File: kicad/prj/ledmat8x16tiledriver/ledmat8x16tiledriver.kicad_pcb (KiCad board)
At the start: 4 copper layers, 31.9 x 31.9 mm, 15 parts, among them J3 Conn_02x08_Odd_Even, J4 Conn_02x08_Odd_Even, U2 DMP31D7LDW, U3 DMP31D7LDW, U4 DMP31D7LDW, U5 DMP31D7LDW

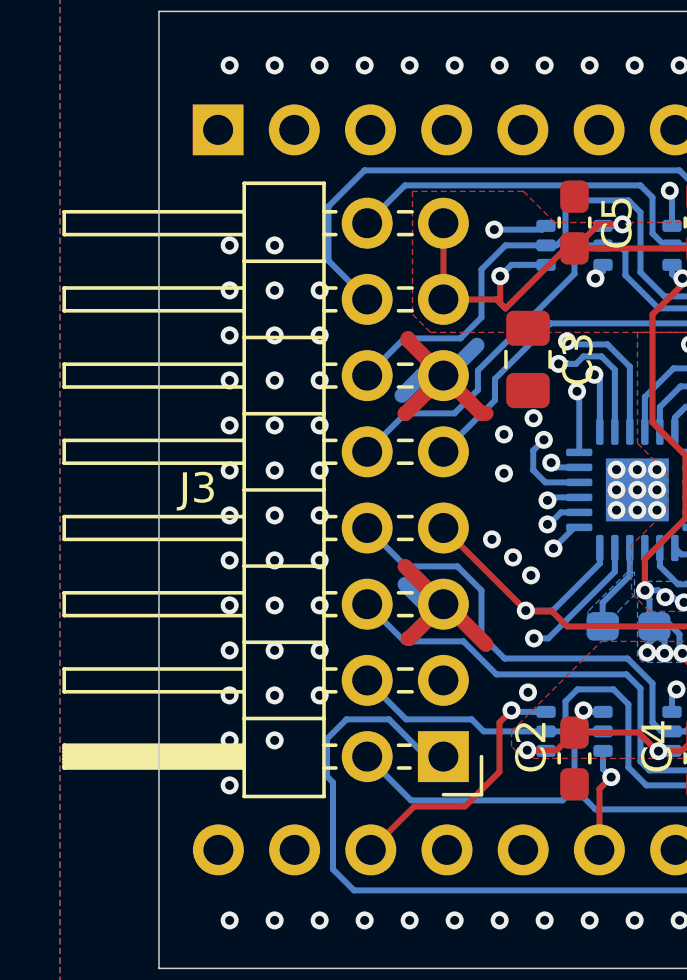
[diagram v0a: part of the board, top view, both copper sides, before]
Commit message: Update footprints in layout (including the led matrix module one)
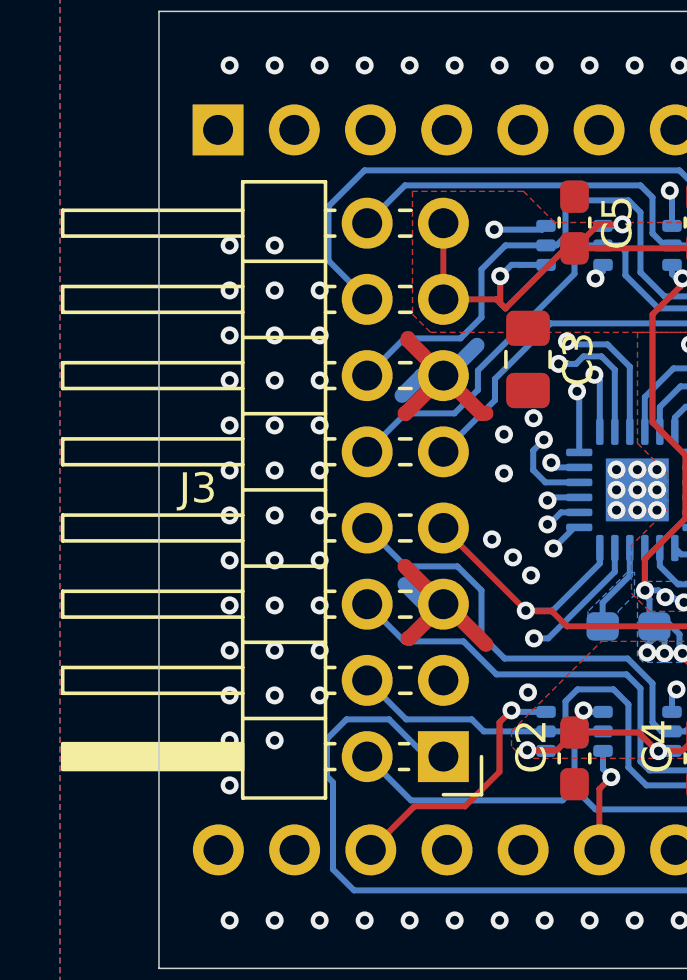
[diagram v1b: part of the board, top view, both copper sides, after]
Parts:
- U1: value ~ -> TLC59283

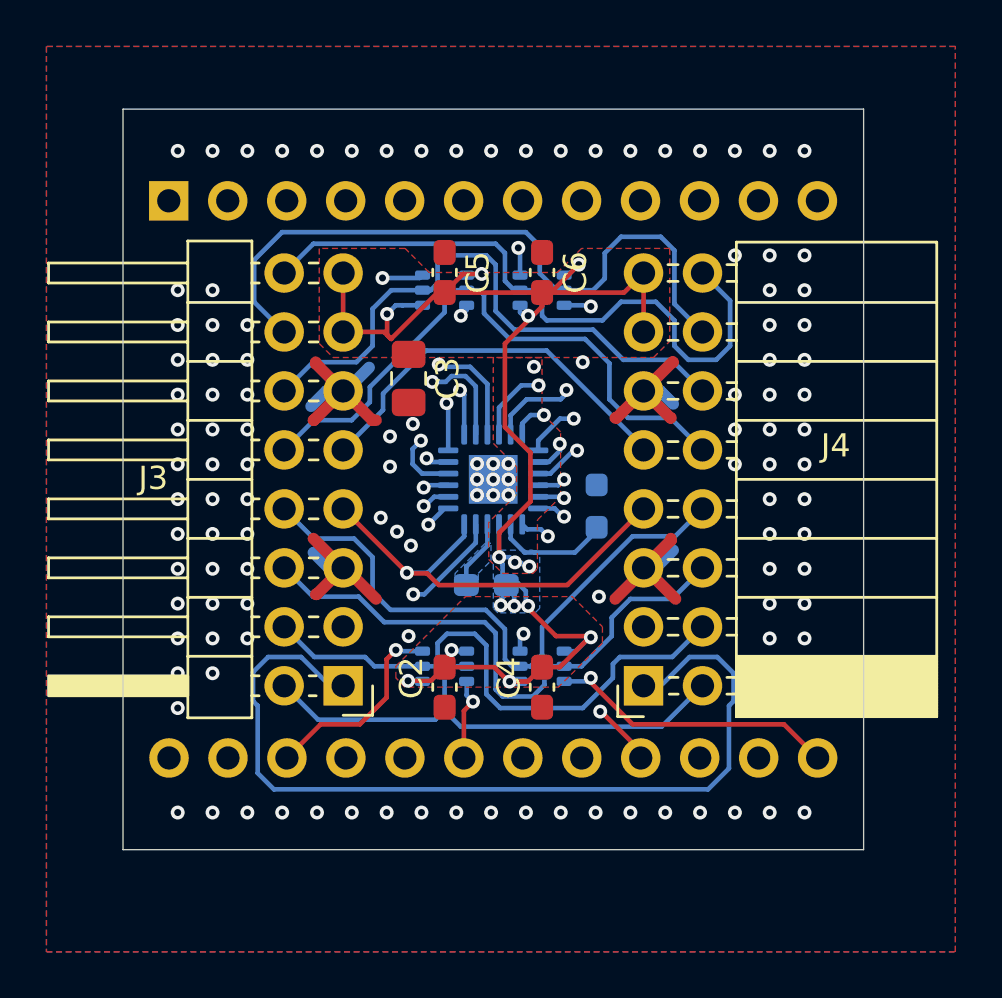
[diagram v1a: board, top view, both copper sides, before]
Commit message: Cut little arcs into the corners for mounting modules with maybe M3 screws
Or perhaps standoffs?
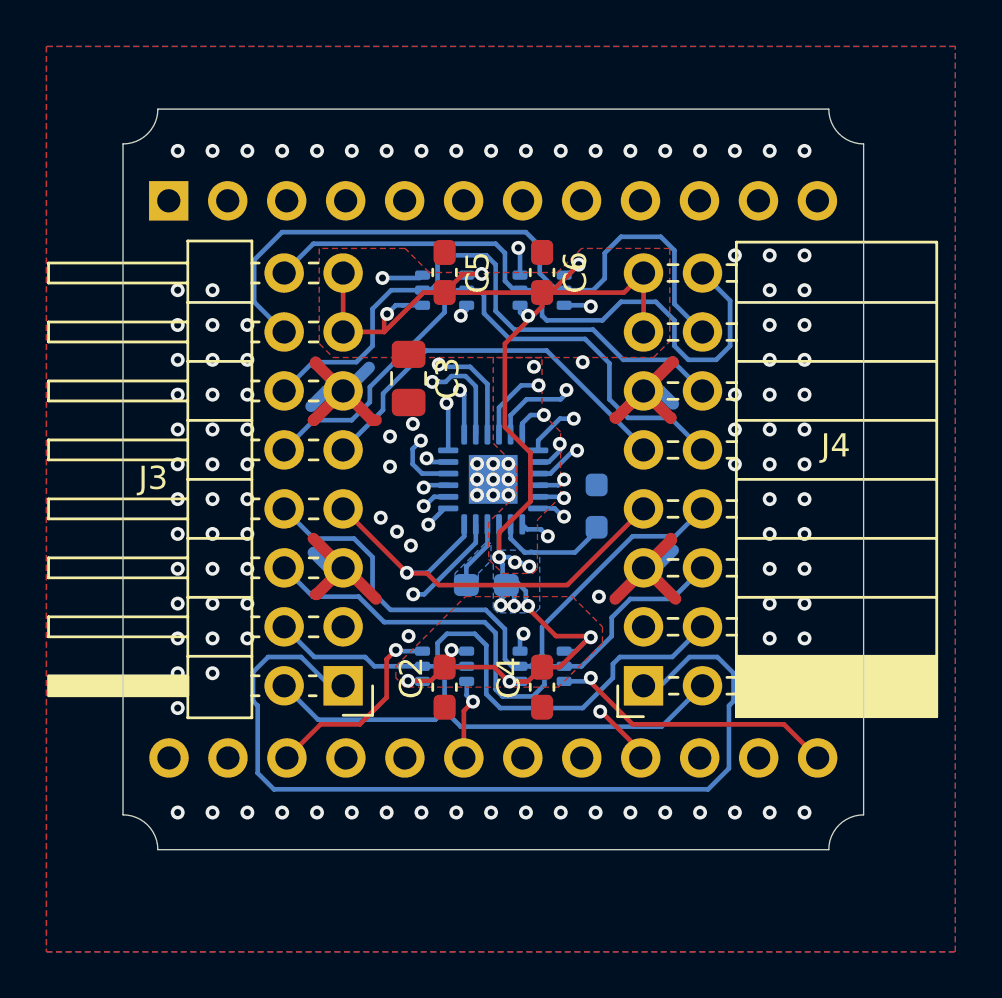
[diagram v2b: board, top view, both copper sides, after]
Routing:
- net +5V: track 67.2 -> 66.6 mm
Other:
- outline, holes or cut-outs redrawn
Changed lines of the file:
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@@
 		(descr "LED matrix tile 8x16 (dual-color)")
 		(property "Reference" "DS1"
-			(at -13.65 -14.45 180)
+			(at -12.65 -14.35 180)
 			(unlocked yes)
 			(layer "B.SilkS")
@@
 		)
 	)
-	(gr_rect
-		(start 129.15 59.2)
-		(end 161.05 91.1)
+	(gr_arc
+		(start 161.05 60.7)
+		(mid 159.98934 60.26066)
+		(end 159.55 59.2)
 		(stroke
 			(width 0.05)
-			(type solid)
-		)
-		(fill no)
+			(type default)
+		)
+		(layer "Edge.Cuts")
+	)
+	(gr_arc
+		(start 130.65 59.2)
+		(mid 130.21066 60.26066)
+		(end 129.15 60.7)
+		(stroke
+			(width 0.05)
+			(type default)
+		)
+		(layer "Edge.Cuts")
+	)
+	(gr_line
+		(start 159.55 91.1)
+		(end 130.65 91.1)
+		(stroke
+			(width 0.05)
+			(type default)
+		)
+		(layer "Edge.Cuts")
+	)
+	(gr_line
+		(start 129.15 89.6)
+		(end 129.15 60.7)
+		(stroke
+			(width 0.05)
+			(type default)
+		)
+		(layer "Edge.Cuts")
+	)
+	(gr_line
+		(start 130.65 59.2)
+		(end 159.55 59.2)
+		(stroke
+			(width 0.05)
+			(type default)
+		)
+		(layer "Edge.Cuts")
+	)
+	(gr_line
+		(start 161.05 60.7)
+		(end 161.05 89.6)
+		(stroke
+			(width 0.05)
+			(type default)
+		)
+		(layer "Edge.Cuts")
+	)
+	(gr_arc
+		(start 129.15 89.6)
+		(mid 130.21066 90.03934)
+		(end 130.65 91.1)
+		(stroke
+			(width 0.05)
+			(type default)
+		)
+		(layer "Edge.Cuts")
+	)
+	(gr_arc
+		(start 159.55 91.1)
+		(mid 159.98934 90.03934)
+		(end 161.05 89.6)
+		(stroke
+			(width 0.05)
+			(type default)
+		)
 		(layer "Edge.Cuts")
 	)
@@
 	)
 	(segment
-		(start 142.7 67.1)
-		(end 143 67.1)
-		(width 0.2)
-		(layer "F.Cu")
-		(net 2)
-	)
-	(segment
 		(start 149.3 81.951473)
 		(end 149.248527 81.9)
@@
 	)
 	(segment
+		(start 142.1 67.1)
+		(end 140.4 68.8)
+		(width 0.2)
+		(layer "F.Cu")
+		(net 2)
+	)
+	(segment
 		(start 145.35 78.5)
 		(end 145.35 77.45)
@@
 	)
 	(segment
-		(start 140.4 68.8)
-		(end 140.7 69.1)
-		(width 0.2)
-		(layer "F.Cu")
-		(net 2)
-	)
-	(segment
 		(start 145.1375 83.2375)
 		(end 143 83.2375)
@@
 	)
 	(segment
-		(start 140.524265 68.924265)
-		(end 140.7 69.1)
-		(width 0.2)
-		(layer "F.Cu")
-		(net 2)
-	)
-	(segment
-		(start 140.7 69.1)
-		(end 142.7 67.1)
+		(start 143 67.1)
+		(end 142.1 67.1)
 		(width 0.2)
 		(layer "F.Cu")
@@
 	)
 	(segment
-		(start 140.524265 68.024265)
-		(end 140.524265 68.924265)
-		(width 0.2)
-		(layer "F.Cu")
-		(net 2)
-	)
-	(segment
 		(start 145.75792 83.85792)
 		(end 145.1375 83.2375)
@@
 	)
 	(segment
+		(start 140.4 68.14853)
+		(end 140.524265 68.024265)
+		(width 0.2)
+		(layer "F.Cu")
+		(net 2)
+	)
+	(segment
 		(start 147.9625 83.2375)
 		(end 147.2 83.2375)
@@
 		(width 0.2)
 		(layer "F.Cu")
+		(net 2)
+	)
+	(segment
+		(start 140.4 68.8)
+		(end 140.4 68.14853)
+		(width 0.2)
+		(layer "F.Cu")

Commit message: Add some holes for headers near the top/bottom edge
Perhaps this can be used as a different way of mounting. Not sure, I'll
have to try. Unfortunately the board dimensions did not allow for the
spacing to be a multiple of 2.54mm. But positioning is such that between
adjacent rows the headers should be exactly 2.54mm apart.
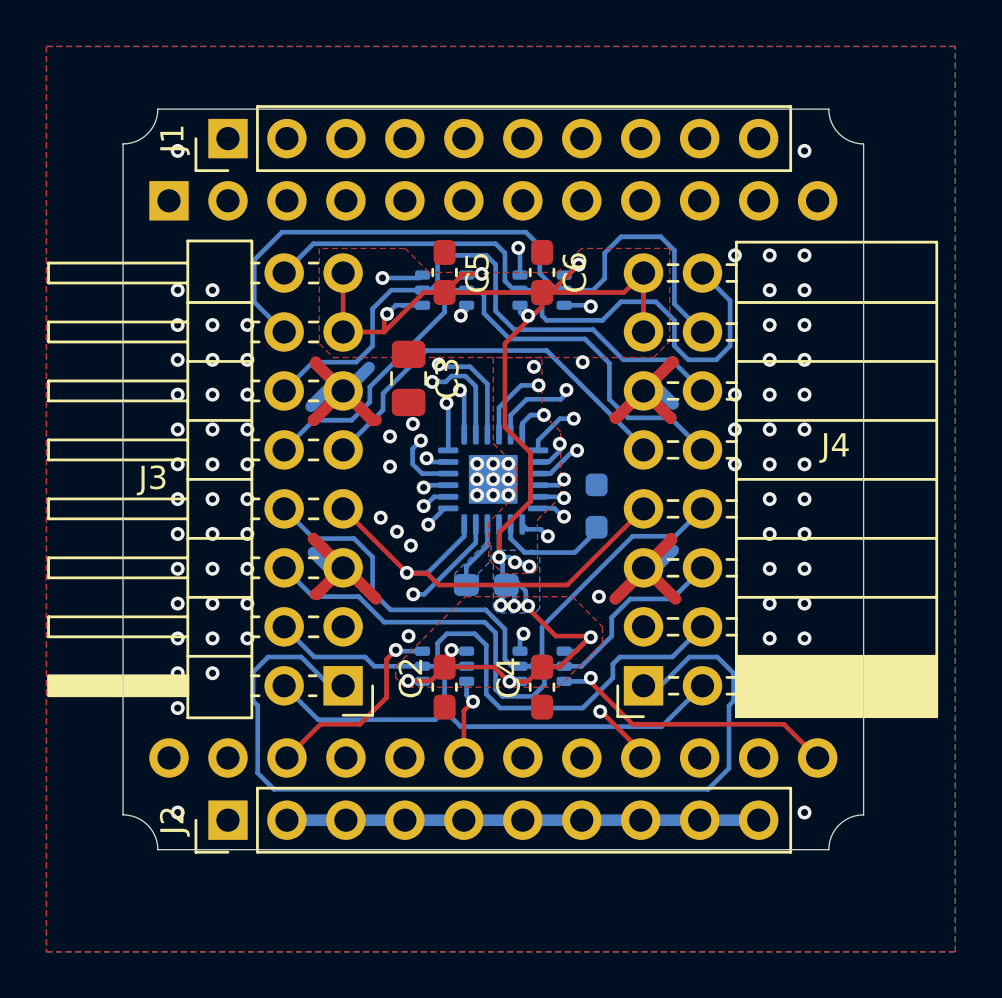
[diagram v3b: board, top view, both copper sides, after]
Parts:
- added J1: Conn_01x10_Pin, Connector_PinHeader_2.54mm:PinHeader_1x10_P2.54mm_Vertical, F.Cu at (133.7, 60.5)
- added J2: Conn_01x10_Pin, Connector_PinHeader_2.54mm:PinHeader_1x10_P2.54mm_Vertical, F.Cu at (133.7, 89.8)
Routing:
- net GND: track 32.4 -> 52.7 mm, vias 124 -> 90

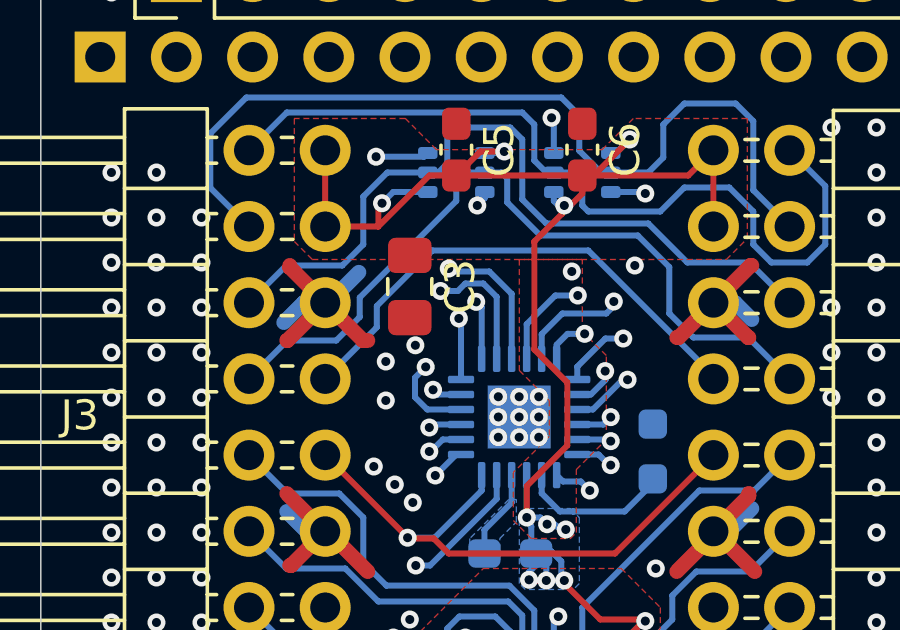
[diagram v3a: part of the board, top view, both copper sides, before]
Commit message: Slight adjustments to zone fill and ground plane
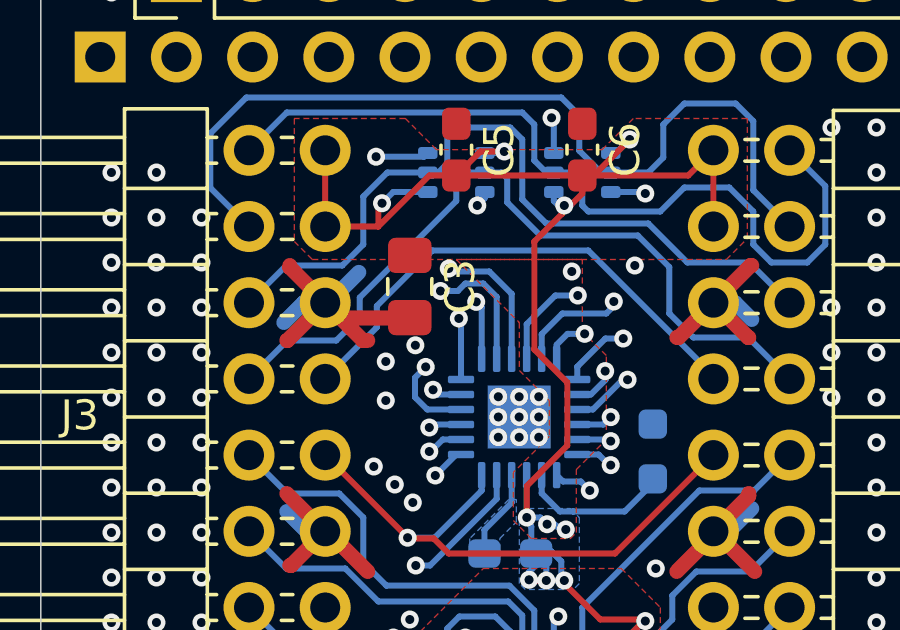
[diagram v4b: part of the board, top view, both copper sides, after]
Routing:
- net GND: track 52.7 -> 55.8 mm
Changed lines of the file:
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@@
 	)
 	(segment
+		(start 141.4375 71.85)
+		(end 141.45 71.8375)
+		(width 0.5)
+		(layer "F.Cu")
+		(net 1)
+	)
+	(segment
 		(start 151.57 71.34)
 		(end 152.73 72.5)
@@
 	)
 	(segment
+		(start 139.14 71.85)
+		(end 141.4375 71.85)
+		(width 0.5)
+		(layer "F.Cu")
+		(net 1)
+	)
+	(segment
 		(start 137.49 80.1)
 		(end 137.45 80.1)
@@
 	)
 	(segment
+		(start 138.63 71.34)
+		(end 139.14 71.85)
+		(width 0.5)
+		(layer "F.Cu")
+		(net 1)
+	)
+	(segment
 		(start 151.57 78.96)
 		(end 151.61 78.96)
@@
 		(polygon
 			(pts
-				(xy 145.1 69.9) (xy 145.1 73.6) (xy 146.1 74.6) (xy 146.1 75.8) (xy 144.9 77) (xy 144.9 78.6) (xy 145.5 79.2)
-				(xy 146.8 79.2) (xy 147 79) (xy 147 76.9) (xy 148 75.9) (xy 148 73.1) (xy 147.2 72.3) (xy 147.2 69.9)
+				(xy 143 69.9) (xy 145.1 72) (xy 145.1 73.6) (xy 146.1 74.6) (xy 146.1 75.8) (xy 144.9 77) (xy 144.9 78.6)
+				(xy 145.5 79.2) (xy 146.8 79.2) (xy 147 79) (xy 147 76.9) (xy 148 75.9) (xy 148 73.1) (xy 147.2 72.3)
+				(xy 147.2 69.9)
 			)
 		)
